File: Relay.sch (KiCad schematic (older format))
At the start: 11 parts

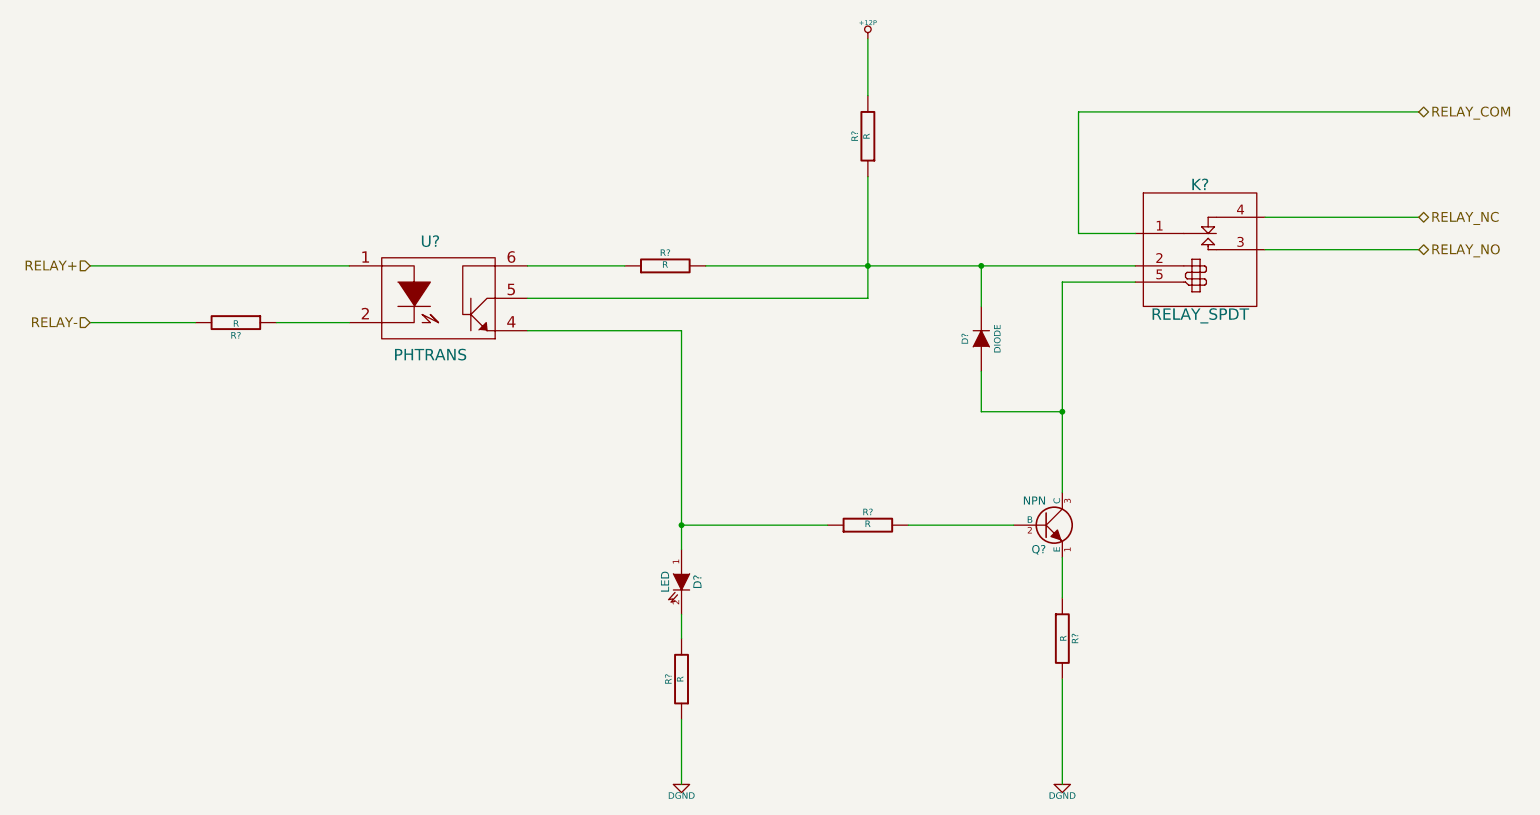
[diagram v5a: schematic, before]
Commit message: started associating relay parts
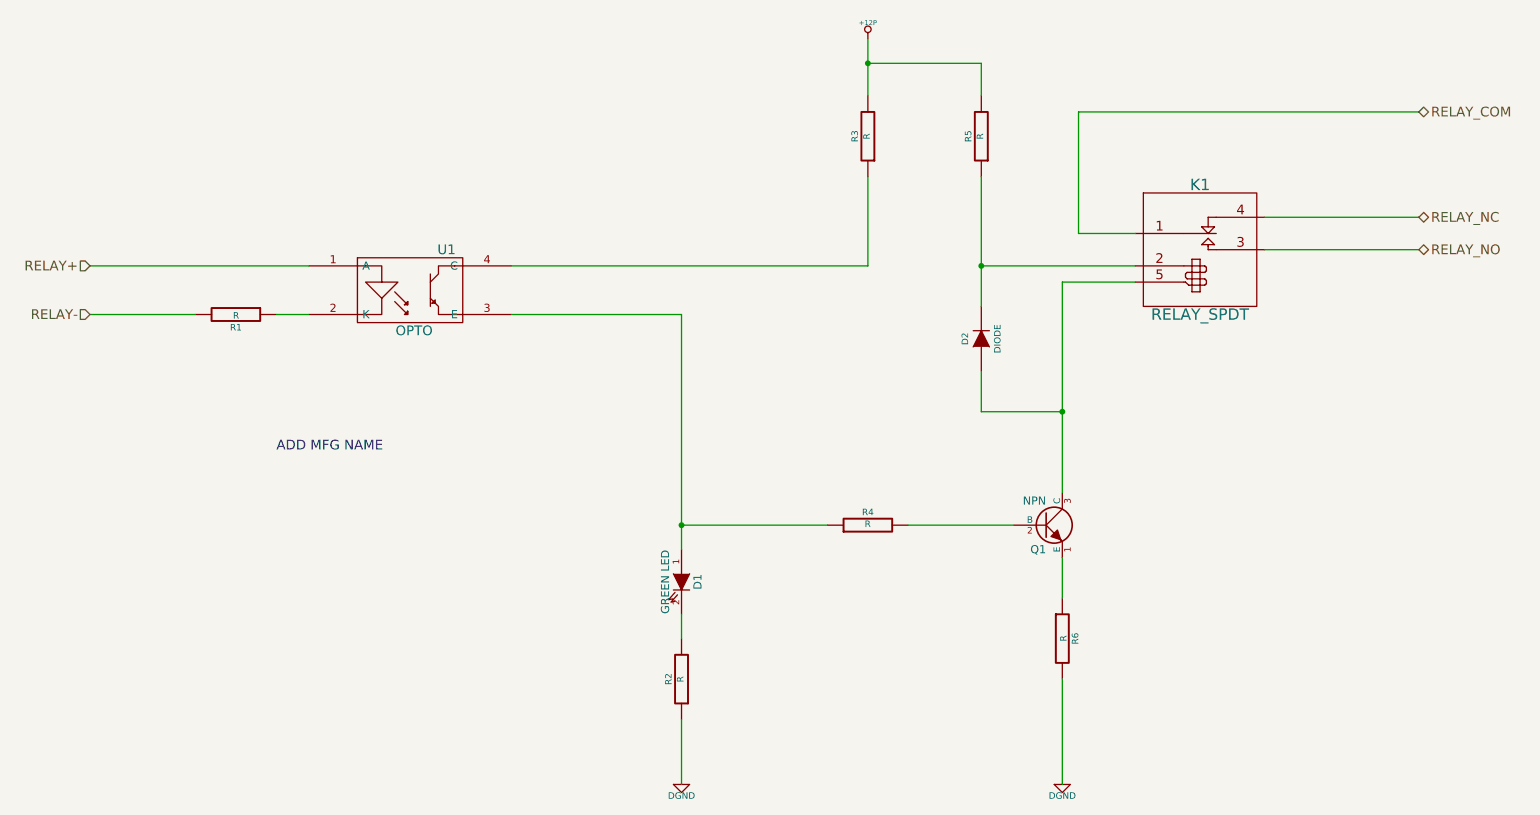
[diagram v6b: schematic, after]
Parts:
- removed R?: R, ~, symbol R
- removed U?: PHTRANS, ~, symbol PHTRANS
- added R5: R, ~, symbol R
- added U1: OPTO, symbol OPTO-TRANSISTOR4
- D1: renamed from D?; value LED -> GREEN LED; Part Number (none) -> LG Q971-KN-1
- D2: renamed from D?; Part Number (none) -> B130-13-F
- K1: renamed from K?; Part Number (none) -> 1461069-5
- Q1: renamed from Q?; Part Number (none) -> MMBT3904-7-F
- gave numbers to parts that had none: 5
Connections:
- net +12P: now also R5.2
- net RELAY+: now also U1.1 (A)
- net at R1.1: now also U1.2 (K)
- net at D1.1 (A), R4.1: now also U1.3 (E)
- net at D2.2 (K), K1.2 (COIL+): now also R5.1; no longer R3.1
- new net: R3.1, U1.4 (C)
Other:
- note added: "ADD MFG NAME"
- moved on the sheet: R1
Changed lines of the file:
@@
 $Descr A4 11693 8268
 encoding utf-8
-Sheet 7 9
+Sheet 5 9
 Title ""
-Date "17 feb 2014"
+Date "20 feb 2014"
 Rev ""
 Comp ""
@@
 Text HLabel 1550 3550 0    60   Input ~ 0
 RELAY+
-Text HLabel 1550 3900 0    60   Input ~ 0
+Text HLabel 1550 3850 0    60   Input ~ 0
 RELAY-
 Text HLabel 9750 3450 2    60   BiDi ~ 0
@@
 RELAY_NC
 $Comp
-L PHTRANS U?
-U 1 1 52F65C85
-P 3700 3750
-F 0 "U?" H 3650 4100 70  0000 C CNN
-F 1 "PHTRANS" H 3650 3400 70  0000 C CNN
-F 2 "~" H 3700 3750 60  0000 C CNN
-F 3 "~" H 3700 3750 60  0000 C CNN
-	1    3700 3750
-	1    0    0    -1
-$EndComp
-$Comp
-L R R?
+L R R4
 U 1 1 52F65C9E
 P 6350 5150
-F 0 "R?" V 6430 5150 40  0000 C CNN
+F 0 "R4" V 6430 5150 40  0000 C CNN
 F 1 "R" V 6357 5151 40  0000 C CNN
 F 2 "~" V 6280 5150 30  0000 C CNN
@@
 $EndComp
 $Comp
-L NPN Q?
+L NPN Q1
 U 1 1 52F65CAD
 P 7450 5150
-F 0 "Q?" H 7450 5000 50  0000 R CNN
+F 0 "Q1" H 7450 5000 50  0000 R CNN
 F 1 "NPN" H 7450 5300 50  0000 R CNN
 F 2 "~" H 7450 5150 60  0000 C CNN
 F 3 "~" H 7450 5150 60  0000 C CNN
+F 4 "MMBT3904-7-F" H 7450 5150 60  0001 C CNN "Part Number"
 	1    7450 5150
 	1    0    0    -1
 $EndComp
 $Comp
-L LED D?
+L LED D1
 U 1 1 52F65CBC
 P 5200 5500
-F 0 "D?" H 5200 5600 50  0000 C CNN
-F 1 "LED" H 5200 5400 50  0000 C CNN
+F 0 "D1" H 5200 5600 50  0000 C CNN
+F 1 "GREEN LED" H 5200 5400 50  0000 C CNN
 F 2 "~" H 5200 5500 60  0000 C CNN
 F 3 "~" H 5200 5500 60  0000 C CNN
+F 4 "LG Q971-KN-1" H 5200 5500 60  0001 C CNN "Part Number"
 	1    5200 5500
 	0    1    1    0
 $EndComp
 $Comp
-L RELAY_SPDT K?
+L RELAY_SPDT K1
 U 1 1 52F663F3
 P 8400 3300
-F 0 "K?" H 8400 3550 70  0000 C CNN
+F 0 "K1" H 8400 3550 70  0000 C CNN
 F 1 "RELAY_SPDT" H 8400 2750 70  0000 C CNN
 F 2 "~" H 8400 3300 60  0000 C CNN
 F 3 "~" H 8400 3300 60  0000 C CNN
+F 4 "1461069-5" H 8400 3300 60  0001 C CNN "Part Number"
 	1    8400 3300
 	1    0    0    -1
@@
 RELAY_COM
 $Comp
-L R R?
+L R R6
 U 1 1 52F665DD
 P 7550 5850
-F 0 "R?" V 7630 5850 40  0000 C CNN
+F 0 "R6" V 7630 5850 40  0000 C CNN
 F 1 "R" V 7557 5851 40  0000 C CNN
 F 2 "~" V 7480 5850 30  0000 C CNN
@@
 $EndComp
 $Comp
-L DGND #PWR?
+L DGND #PWR027
 U 1 1 52F665ED
 P 7550 6750
-F 0 "#PWR?" H 7550 6750 40  0001 C CNN
+F 0 "#PWR027" H 7550 6750 40  0001 C CNN
 F 1 "DGND" H 7550 6680 40  0000 C CNN
 F 2 "" H 7550 6750 60  0000 C CNN
@@
 $EndComp
 $Comp
-L R R?
+L R R3
 U 1 1 52F66784
 P 6350 2750
-F 0 "R?" V 6430 2750 40  0000 C CNN
+F 0 "R3" V 6430 2750 40  0000 C CNN
 F 1 "R" V 6357 2751 40  0000 C CNN
 F 2 "~" V 6280 2750 30  0000 C CNN
@@
 $EndComp
 $Comp
-L R R?
-U 1 1 52F66924
-P 5100 3550
-F 0 "R?" V 5180 3550 40  0000 C CNN
-F 1 "R" V 5107 3551 40  0000 C CNN
-F 2 "~" V 5030 3550 30  0000 C CNN
-F 3 "~" H 5100 3550 30  0000 C CNN
-	1    5100 3550
-	0    -1   -1   0
-$EndComp
-$Comp
-L R R?
+L R R2
 U 1 1 52F66991
 P 5200 6100
-F 0 "R?" V 5280 6100 40  0000 C CNN
+F 0 "R2" V 5280 6100 40  0000 C CNN
 F 1 "R" V 5207 6101 40  0000 C CNN
 F 2 "~" V 5130 6100 30  0000 C CNN
@@
 	-1   0    0    1
 $EndComp
-Wire Wire Line
-	9750 2600 7650 2600
-Wire Wire Line
-	7650 2600 7650 3350
-Wire Wire Line
-	7650 3350 8000 3350
-Wire Wire Line
-	9750 3250 8800 3250
-Wire Wire Line
-	8800 3450 9750 3450
-Wire Wire Line
-	8000 3650 7550 3650
-Wire Wire Line
-	7550 3650 7550 4950
-Wire Wire Line
-	7550 6750 7550 6100
-Wire Wire Line
-	7550 5600 7550 5350
-Wire Wire Line
-	6600 5150 7250 5150
-Wire Wire Line
-	6350 2500 6350 2150
-Wire Wire Line
-	6350 3000 6350 3750
-Wire Wire Line
-	4850 3550 4250 3550
-Wire Wire Line
-	5350 3550 8000 3550
-Wire Wire Line
-	6350 3750 4250 3750
-Connection ~ 6350 3550
-Wire Wire Line
-	5200 3950 5200 5300
-Wire Wire Line
-	5200 5850 5200 5700
-$Comp
-L DGND #PWR?
+$Comp
+L DGND #PWR028
 U 1 1 52F669C7
 P 5200 6750
-F 0 "#PWR?" H 5200 6750 40  0001 C CNN
+F 0 "#PWR028" H 5200 6750 40  0001 C CNN
 F 1 "DGND" H 5200 6680 40  0000 C CNN
 F 2 "" H 5200 6750 60  0000 C CNN
@@
 	1    0    0    -1
 $EndComp
-Wire Wire Line
-	5200 6750 5200 6350
-Wire Wire Line
-	1550 3550 3150 3550
-$Comp
-L R R?
+$Comp
+L R R1
 U 1 1 52F66A05
-P 2450 3900
-F 0 "R?" V 2530 3900 40  0000 C CNN
-F 1 "R" V 2457 3901 40  0000 C CNN
-F 2 "~" V 2380 3900 30  0000 C CNN
-F 3 "~" H 2450 3900 30  0000 C CNN
-	1    2450 3900
+P 2450 3850
+F 0 "R1" V 2530 3850 40  0000 C CNN
+F 1 "R" V 2457 3851 40  0000 C CNN
+F 2 "~" V 2380 3850 30  0000 C CNN
+F 3 "~" H 2450 3850 30  0000 C CNN
+	1    2450 3850
 	0    1    1    0
 $EndComp
-Wire Wire Line
-	2700 3900 3150 3900
-Wire Wire Line
-	2200 3900 1550 3900
-Wire Wire Line
-	4250 3950 5200 3950
-Wire Wire Line
-	5200 5150 6100 5150
-Connection ~ 5200 5150
-$Comp
-L DIODE D?
+$Comp
+L DIODE D2
 U 1 1 52F66DA7
 P 7050 4000
-F 0 "D?" H 7050 4100 40  0000 C CNN
+F 0 "D2" H 7050 4100 40  0000 C CNN
 F 1 "DIODE" H 7050 3900 40  0000 C CNN
 F 2 "~" H 7050 4000 60  0000 C CNN
 F 3 "~" H 7050 4000 60  0000 C CNN
+F 4 "B130-13-F" H 7050 4000 60  0001 C CNN "Part Number"
 	1    7050 4000
 	0    -1   -1   0
 $EndComp
-Wire Wire Line
-	7050 3800 7050 3550
-Connection ~ 7050 3550
-Wire Wire Line
-	7050 4200 7050 4450
-Wire Wire Line
-	7050 4450 7550 4450
-Connection ~ 7550 4450
-$Comp
-L +12P #PWR?
+$Comp
+L +12P #PWR029
 U 1 1 52F6868D
 P 6350 2150
-F 0 "#PWR?" H 6350 2120 30  0001 C CNN
+F 0 "#PWR029" H 6350 2120 30  0001 C CNN
 F 1 "+12P" H 6350 2250 30  0000 C CNN
 F 2 "" H 6350 2150 60  0000 C CNN
@@
 	1    0    0    -1
 $EndComp
+$Comp
+L OPTO-TRANSISTOR4 U1
+U 1 1 530580F0
+P 3550 3700
+F 0 "U1" H 3750 3950 60  0000 C CNN
+F 1 "OPTO" H 3550 3450 60  0000 C CNN
+F 2 "" H 3550 3700 60  0000 C CNN
+F 3 "" H 3550 3700 60  0000 C CNN
+F 4 "LTV-816S" H 3550 3700 60  0001 C CNN "Part Number"
+	1    3550 3700
+	1    0    0    -1
+$EndComp
+Wire Wire Line
+	9750 2600 7650 2600
+Wire Wire Line
+	7650 2600 7650 3350
+Wire Wire Line
+	7650 3350 8000 3350
+Wire Wire Line
+	9750 3250 8800 3250
+Wire Wire Line
+	8800 3450 9750 3450
+Wire Wire Line
+	8000 3650 7550 3650
+Wire Wire Line
+	7550 3650 7550 4950
+Wire Wire Line
+	7550 6750 7550 6100
+Wire Wire Line
+	7550 5600 7550 5350
+Wire Wire Line
+	6600 5150 7250 5150
+Wire Wire Line
+	6350 2500 6350 2150
+Wire Wire Line
+	5200 3850 5200 5300
+Wire Wire Line
+	5200 5850 5200 5700
+Wire Wire Line
+	5200 6750 5200 6350
+Wire Wire Line
+	1550 3550 2900 3550
+Wire Wire Line
+	2700 3850 2900 3850
+Wire Wire Line
+	2200 3850 1550 3850
+Wire Wire Line
+	4150 3850 5200 3850
+Wire Wire Line
+	5200 5150 6100 5150
+Connection ~ 5200 5150
+Wire Wire Line
+	7050 3000 7050 3800
+Connection ~ 7050 3550
+Wire Wire Line
+	7050 4200 7050 4450
+Wire Wire Line
+	7050 4450 7550 4450
+Connection ~ 7550 4450
+Wire Wire Line
+	6350 3000 6350 3550
+Text Notes 2700 4700 0    60   ~ 0
+ADD MFG NAME
+Wire Wire Line
+	6350 3550 4150 3550
+Wire Wire Line
+	7050 3550 8000 3550
+$Comp
+L R R5
+U 1 1 5305826F
+P 7050 2750
+F 0 "R5" V 7130 2750 40  0000 C CNN
+F 1 "R" V 7057 2751 40  0000 C CNN
+F 2 "~" V 6980 2750 30  0000 C CNN
+F 3 "~" H 7050 2750 30  0000 C CNN
+	1    7050 2750
+	-1   0    0    1
+$EndComp
+Wire Wire Line
+	7050 2500 7050 2300
+Wire Wire Line
+	7050 2300 6350 2300
+Connection ~ 6350 2300
 $EndSCHEMATC

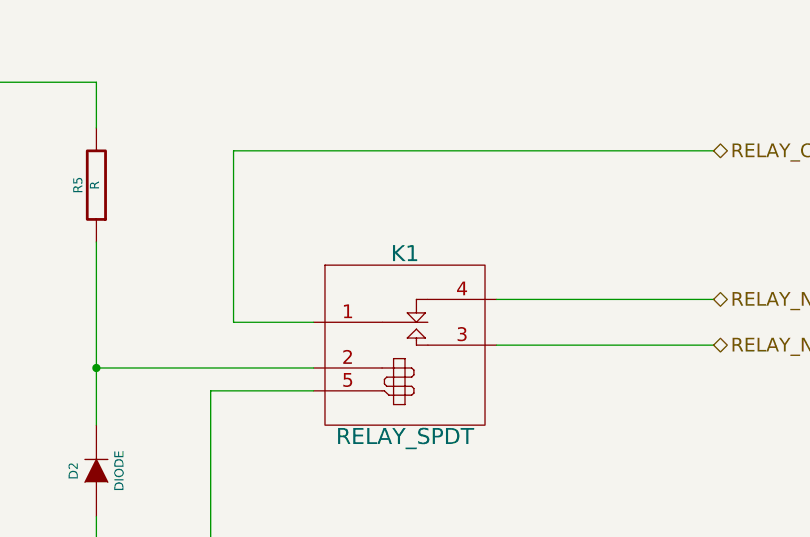
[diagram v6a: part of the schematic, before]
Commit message: worked on associating parts
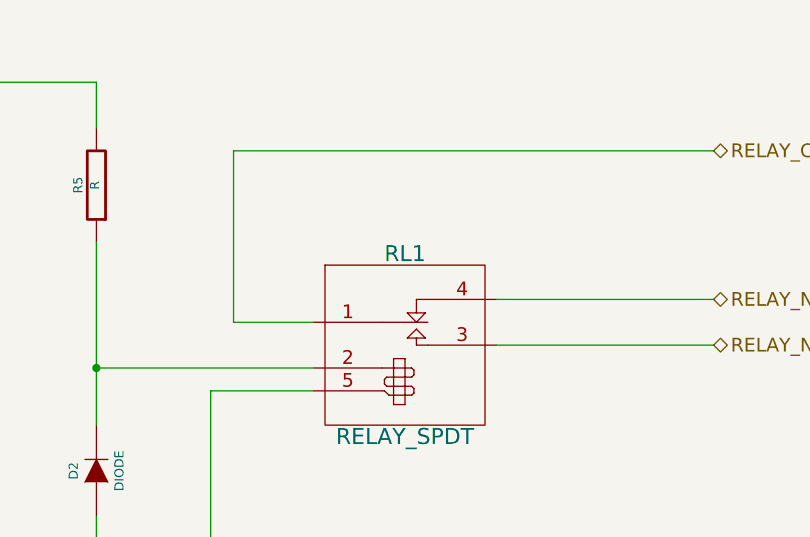
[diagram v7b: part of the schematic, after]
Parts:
- renumbered K1 to RL1
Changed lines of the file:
@@
 Sheet 5 9
 Title ""
-Date "20 feb 2014"
+Date "23 feb 2014"
 Rev ""
 Comp ""
@@
 $EndComp
 $Comp
-L RELAY_SPDT K1
+L RELAY_SPDT RL1
 U 1 1 52F663F3
 P 8400 3300
-F 0 "K1" H 8400 3550 70  0000 C CNN
+F 0 "RL1" H 8400 3550 70  0000 C CNN
 F 1 "RELAY_SPDT" H 8400 2750 70  0000 C CNN
 F 2 "~" H 8400 3300 60  0000 C CNN
@@
 $EndComp
 $Comp
-L DGND #PWR027
+L DGND #PWR42
 U 1 1 52F665ED
 P 7550 6750
-F 0 "#PWR027" H 7550 6750 40  0001 C CNN
+F 0 "#PWR42" H 7550 6750 40  0001 C CNN
 F 1 "DGND" H 7550 6680 40  0000 C CNN
 F 2 "" H 7550 6750 60  0000 C CNN
@@
 $EndComp
 $Comp
-L DGND #PWR028
+L DGND #PWR40
 U 1 1 52F669C7
 P 5200 6750
-F 0 "#PWR028" H 5200 6750 40  0001 C CNN
+F 0 "#PWR40" H 5200 6750 40  0001 C CNN
 F 1 "DGND" H 5200 6680 40  0000 C CNN
 F 2 "" H 5200 6750 60  0000 C CNN
@@
 $EndComp
 $Comp
-L +12P #PWR029
+L +12P #PWR41
 U 1 1 52F6868D
 P 6350 2150
-F 0 "#PWR029" H 6350 2120 30  0001 C CNN
+F 0 "#PWR41" H 6350 2120 30  0001 C CNN
 F 1 "+12P" H 6350 2250 30  0000 C CNN
 F 2 "" H 6350 2150 60  0000 C CNN
